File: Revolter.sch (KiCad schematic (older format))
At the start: 27 parts, among them J2 TEMP, J3 USB_B_Mini, P3 IN+, P4 IN-, P5 MOTOR3, P6 MOTOR2, P7 MOTOR1, Q1 Q_NMOS_GSD, Q2 Q_NMOS_GSD, Q3 Q_NMOS_GSD

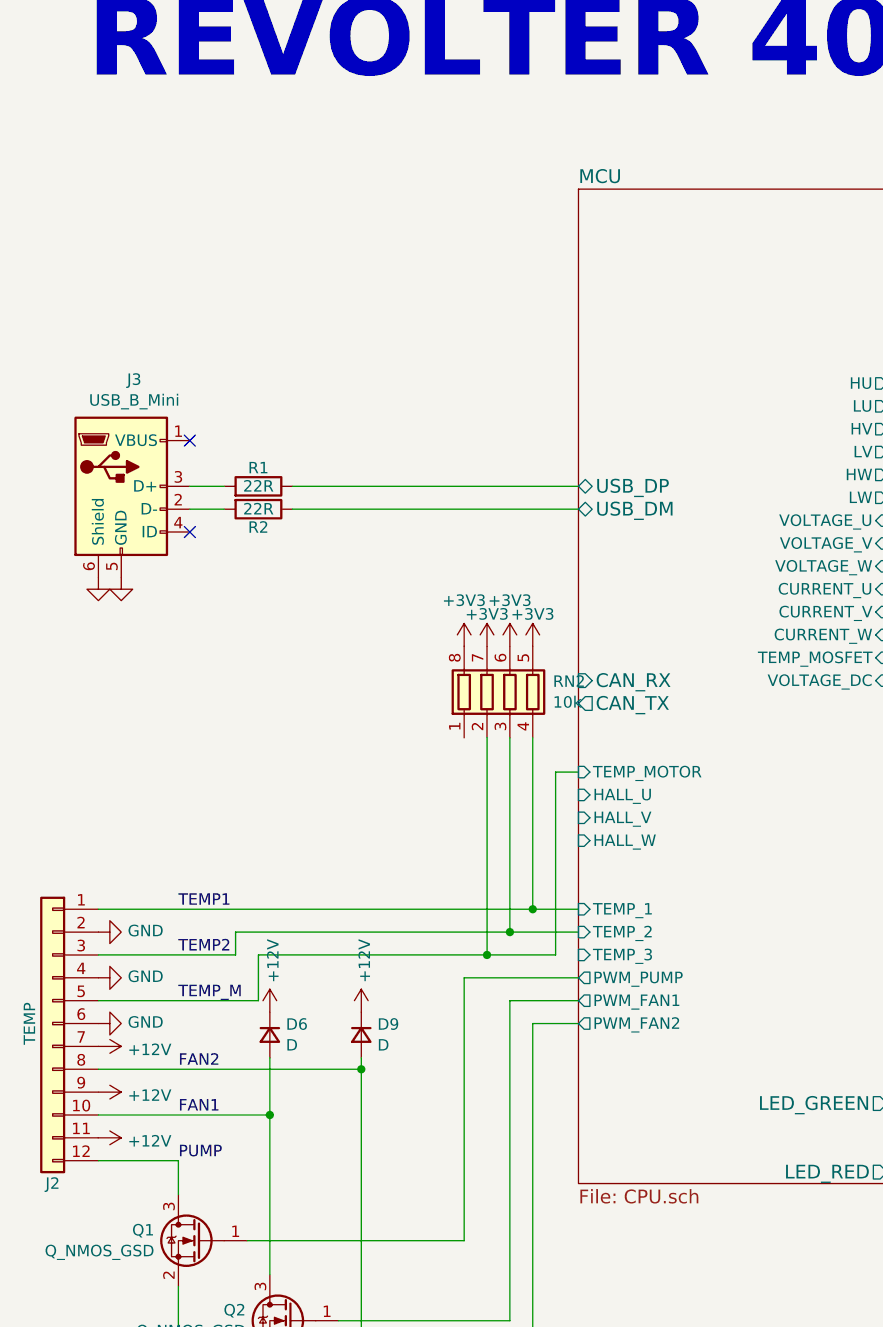
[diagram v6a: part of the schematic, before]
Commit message: - removed Temp3 input - removed hall input - removed CAN - added HMI UART - added freewheeling diode to pump output - moved temp connector left to mitigate collision with USB - added fourth pinhole for pasting
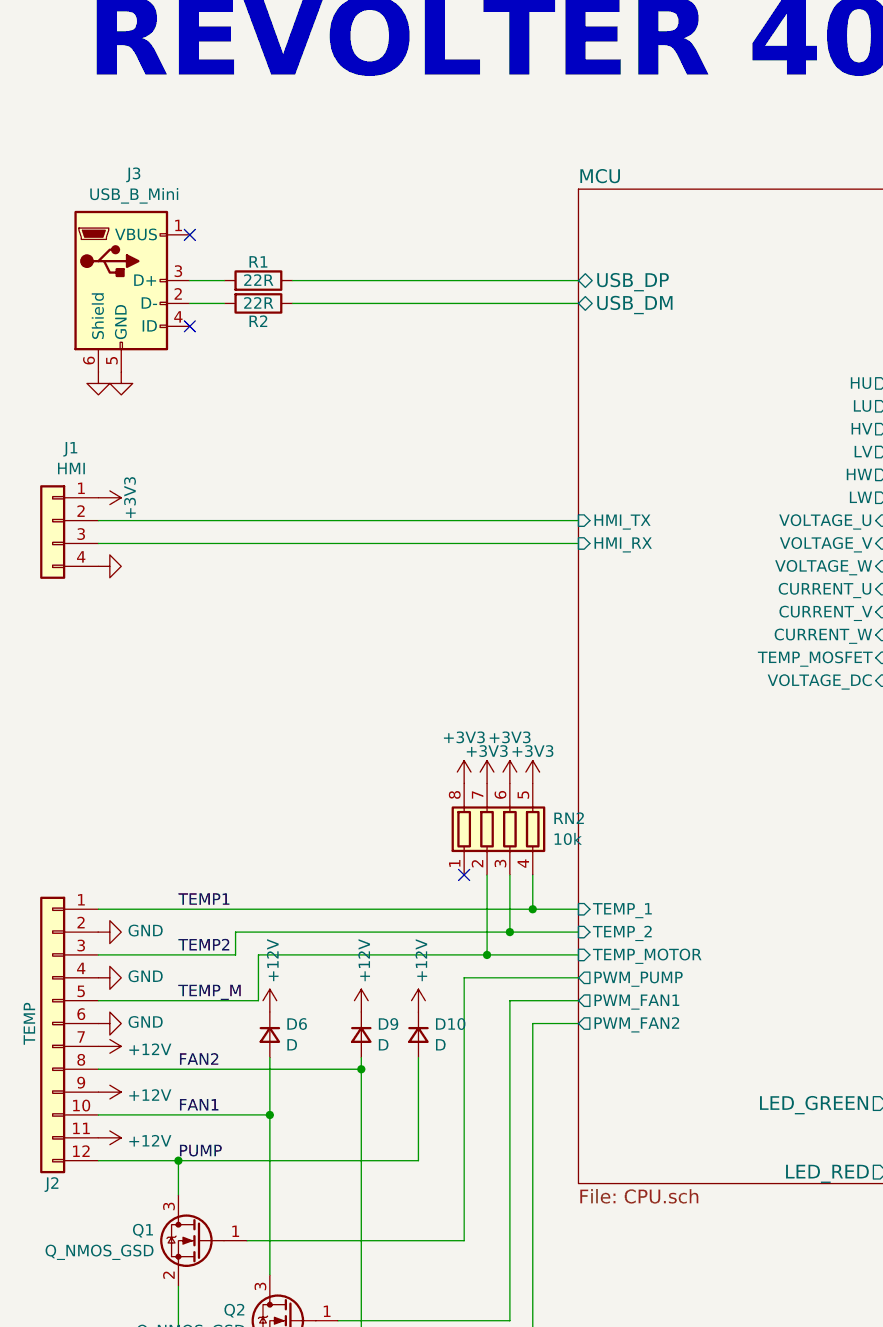
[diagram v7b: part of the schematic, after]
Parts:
- added D10: D, Diode_SMD:D_SOD-123, symbol Device:D_Small
- added J1: HMI, Connector_PinHeader_2.00mm:PinHeader_1x04_P2.00mm_Vertical, symbol Connector_Generic:Conn_01x04
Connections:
- net +12V: now also D10.1 (K)
- net +3V3: now also J1.1 (Pin_1)
- net GND: now also J1.4 (Pin_4)
- net PUMP: now also D10.2 (A)
- new net MCU/HMI_RX: J1.3 (Pin_3)
- new net MCU/HMI_TX: J1.2 (Pin_2)
- no-connect marks 2 -> 3
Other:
- moved on the sheet: J3, R1, R2, RN2

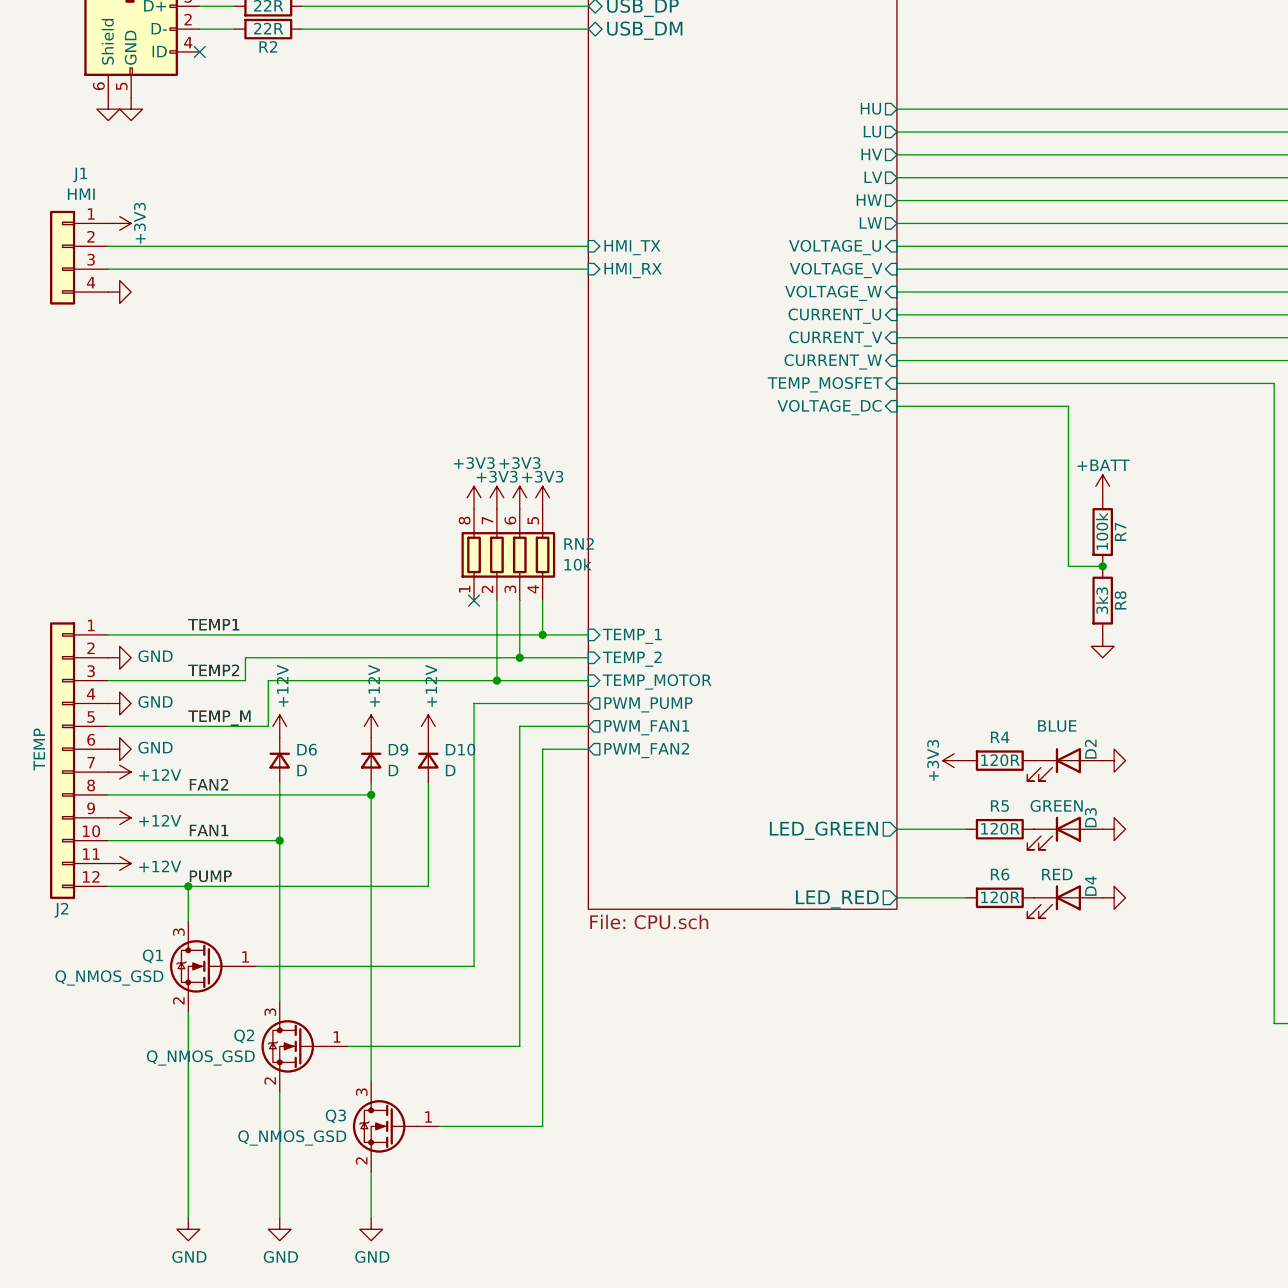
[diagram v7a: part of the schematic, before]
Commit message: - removed one fan output - moved PWM pins to TIM4 - added pull-up to fan output (for 4pin fan) - removed blue power LED - split 12pin to 5 2pin connectors - reduced LED resistors - removed optional current sensor - removed HV DCDC converter - added some cap values
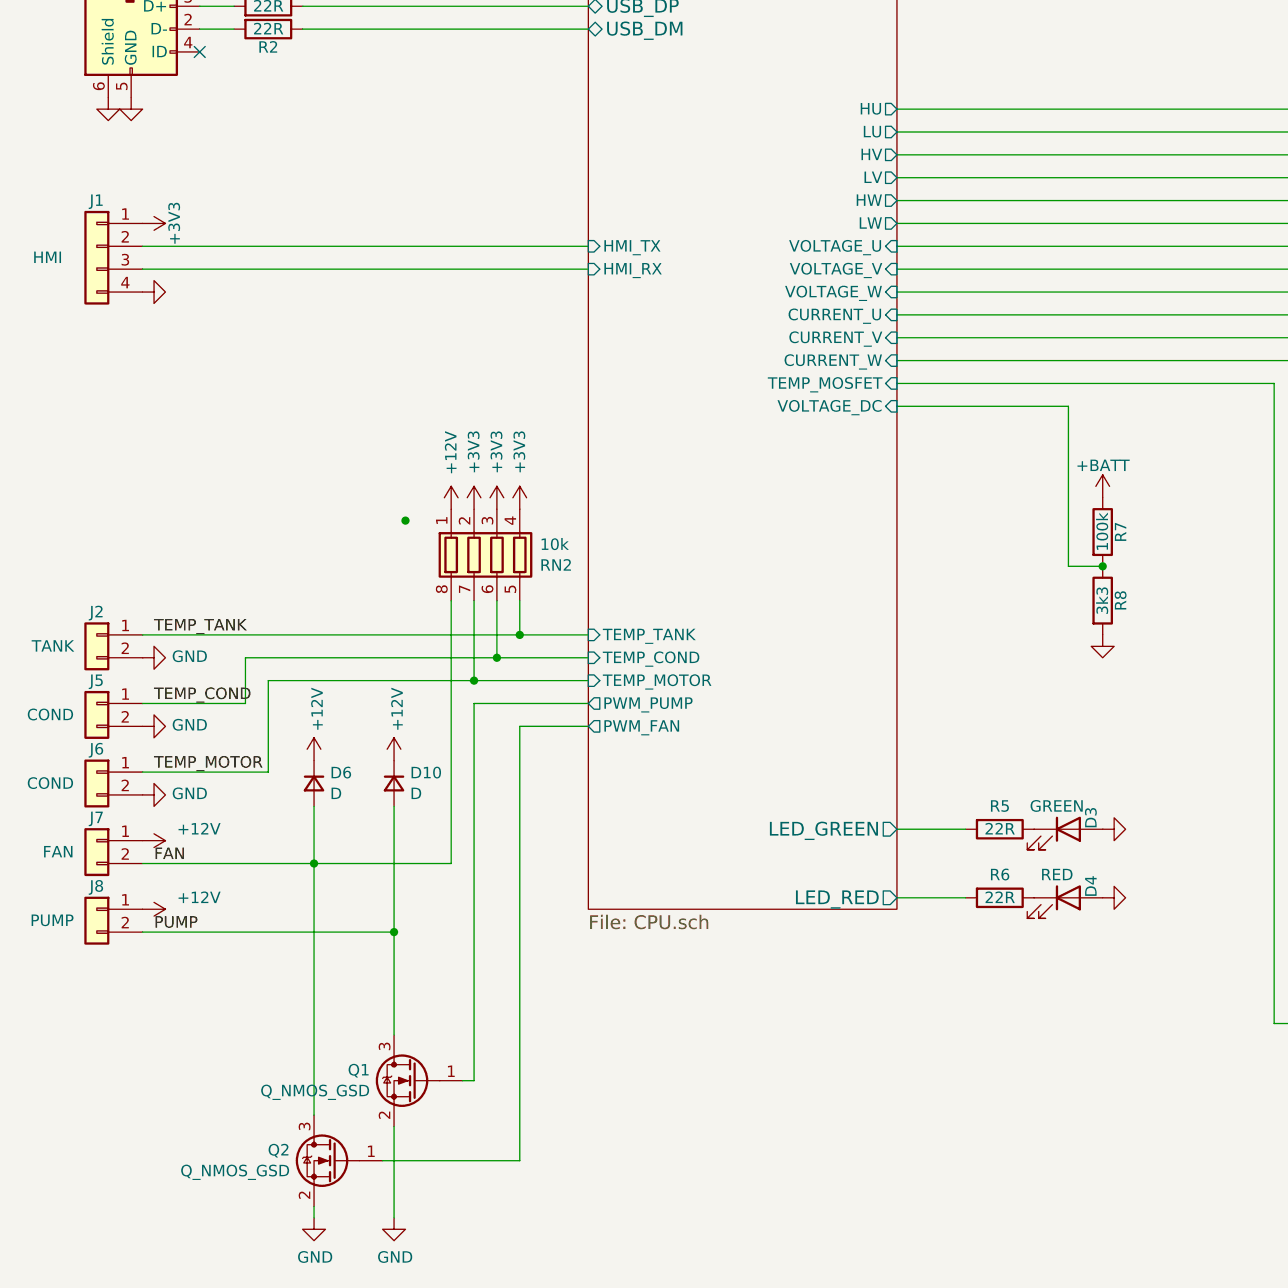
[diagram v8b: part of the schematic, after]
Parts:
- removed D2: BLUE, LED_SMD:LED_0805_2012Metric, symbol Device:LED
- removed D9: D, Diode_SMD:D_SOD-123, symbol Device:D_Small
- removed J2: TEMP, Connector_PinHeader_2.00mm:PinHeader_1x12_P2.00mm_Vertical, symbol Connector_Generic:Conn_01x12
- removed Q3: Q_NMOS_GSD, Package_TO_SOT_SMD:SOT-23, symbol Device:Q_NMOS_GSD
- removed R4: 120R, Resistor_SMD:R_0805_2012Metric, symbol Device:R
- added J2: TANK, Connector_JST:JST_PH_B2B-PH-K_1x02_P2.00mm_Vertical, symbol Connector_Generic:Conn_01x02
- added J5, J6: COND, Connector_JST:JST_PH_B2B-PH-K_1x02_P2.00mm_Vertical, symbol Connector_Generic:Conn_01x02
- added J7: FAN, Connector_JST:JST_PH_B2B-PH-K_1x02_P2.00mm_Vertical, symbol Connector_Generic:Conn_01x02
- added J8: PUMP, Connector_JST:JST_PH_B2B-PH-K_1x02_P2.00mm_Vertical, symbol Connector_Generic:Conn_01x02
- J1: footprint Connector_PinHeader_2.00mm:PinHeader_1x04_P2.00mm_Vertical -> Connector_JST:JST_PH_B4B-PH-K_1x04_P2.00mm_Vertical
- R5, R6: value 120R -> 22R
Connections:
- net TEMP1 is gone; now on net +3V3: RN2.4 (R4.1)
- net TEMP2 is gone; now on net +3V3: RN2.3 (R3.1)
- net TEMP_M is gone; now on net +3V3: RN2.2 (R2.1)
- net +12V: now also RN2.1 (R1.1), J7.1 (Pin_1), J8.1 (Pin_1)
- net +3V3: no longer RN2.5 (R4.2), RN2.6 (R3.2), RN2.7 (R2.2), RN2.8 (R1.2)
- net GND: now also J2.2 (Pin_2), J5.2 (Pin_2), J6.2 (Pin_2)
- net PUMP: now also J8.2 (Pin_2)
- net FAN1 renamed FAN
- net FAN: now also RN2.8 (R1.2), J7.2 (Pin_2)
- net MCU/PWM_FAN1 renamed MCU/PWM_FAN
- new net TEMP_COND: J5.1 (Pin_1), RN2.6 (R3.2)
- new net TEMP_MOTOR: J6.1 (Pin_1), RN2.7 (R2.2)
- new net TEMP_TANK: J2.1 (Pin_1), RN2.5 (R4.2)
- no-connect marks 3 -> 2
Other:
- moved on the sheet: D10, D6, J1, Q1, Q2, RN2
